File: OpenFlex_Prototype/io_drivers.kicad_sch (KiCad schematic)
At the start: 29 parts, among them Q1 IRF740, Q2 IRF740, Q3 IRF740, Q4 IRF740, U1 LM324, U2 TC4424, U3 TC4424

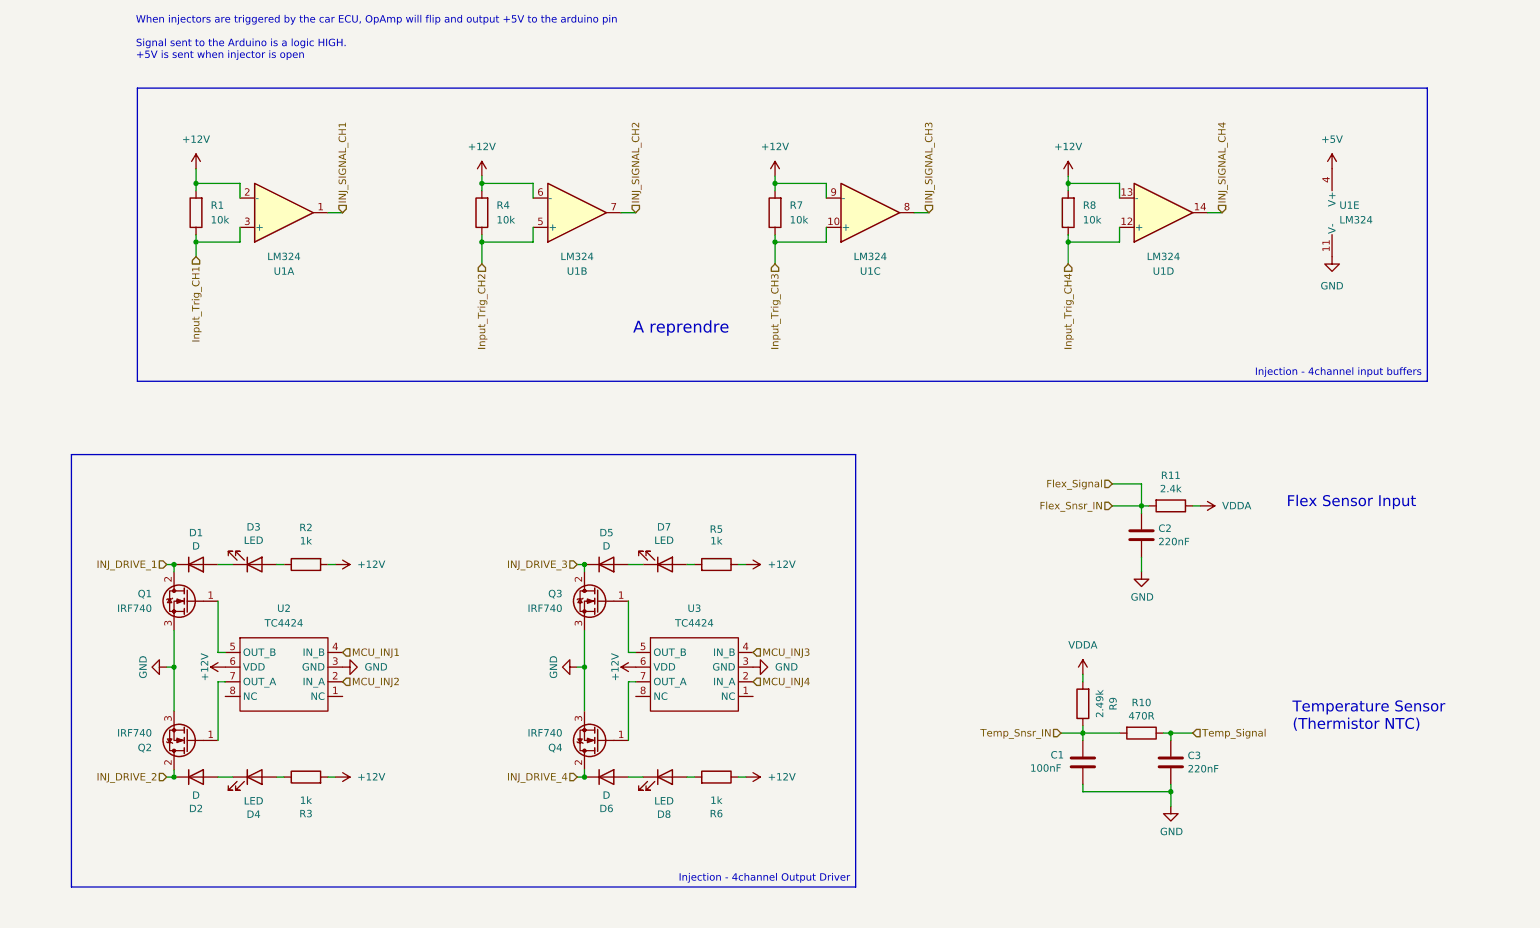
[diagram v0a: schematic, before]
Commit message: Updated PCB to ESP32-S2-Devkit-C1
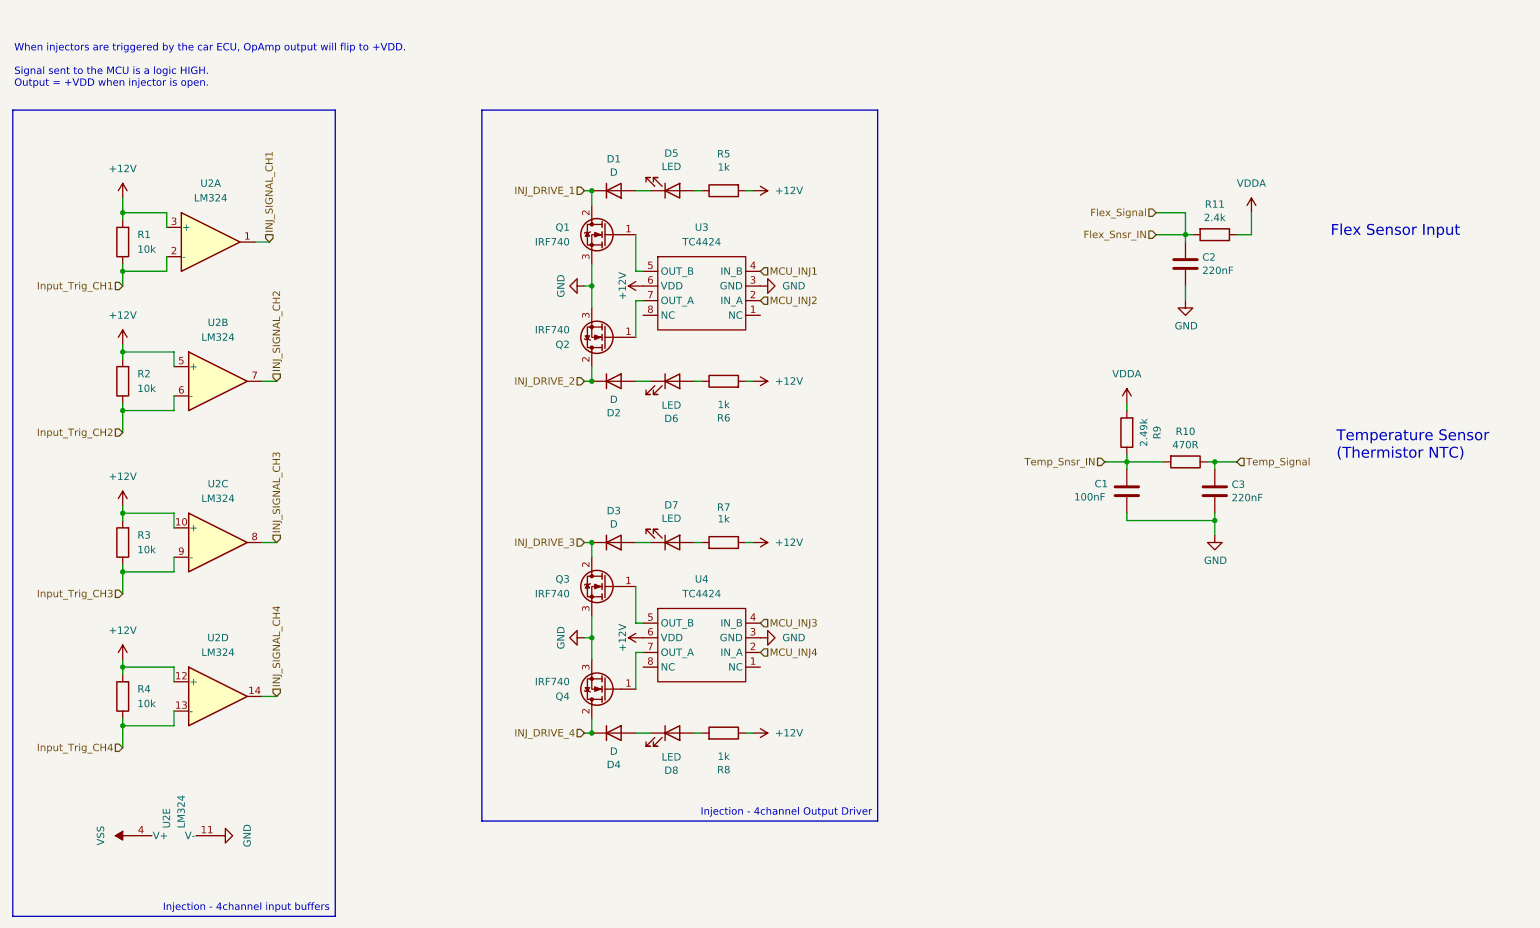
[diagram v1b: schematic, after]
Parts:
- Q1, Q2, Q3, Q4: Manufacturer_Name (none) -> Vishay Semiconductors; Manufacturer_Part_Number (none) -> IRF740PBF; Mouser_Part_Number (none) -> 844-IRF740PBF; URL (none) -> https://www.mouser.fr/ProductDetail/Vishay-Semiconductors/I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
- renumbered D5 to D3, D6 to D4, D3 to D5, D4 to D6, R4 to R2, R7 to R3, R8 to R4, R2 to R5, R3 to R6, R5 to R7, R6 to R8, U1 to U2, U2 to U3, U3 to U4
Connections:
- net +12V: now also U2.10 (+), U2.12 (+), U2.3 (+), U2.5 (+); no longer U2.13 (-), U2.2 (-), U2.6 (-), U2.9 (-)
- net Input_Trig_CH1: now also U2.2 (-); no longer U2.3 (+)
- net Input_Trig_CH2: now also U2.6 (-); no longer U2.5 (+)
- net Input_Trig_CH3: now also U2.9 (-); no longer U2.10 (+)
- net Input_Trig_CH4: now also U2.13 (-); no longer U2.12 (+)
- net +5V renamed VSS
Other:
- note added: "When injectors are triggered by the car ECU, OpAmp output will flip to +VDD. Signal sent to the MCU is a logic HIGH. Output = +VDD when injector is open."
- note removed: "A reprendre"
- note removed: "When injectors are triggered by the car ECU, OpAmp will flip and output +5V to the arduino pin Signal sent to the Arduino is a logic HIGH. +5V is sent when injector is open"
- moved on the sheet: C1, C2, C3, D1, D2, D3, D4, D5, D6, D7, D8, Q4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

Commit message: Updated Sourcing for prototype
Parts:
- C1: Digikey Part Number 445-180563-1-ND -> (none); URL https://www.digikey.com.au/product-detail/en/tdk-corporatio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 -> https://www.mouser.fr/ProductDetail/TDK/FA18X8R1E104KNU06?q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
- C2, C3: Digikey Part Number Digikey Part Number -> (none); URL https://www.digikey.com.au/product-detail/en/tdk-corporatio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 -> https://www.mouser.fr/ProductDetail/TDK/FA18X8R1E224KRU06?q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
- D7: Digikey Part Number 732-5005-ND -> (none)
- R1, R2, R3, R4: Manufacturer_Name (none) -> YAGEO; Manufacturer_Part_Number (none) -> MFR-25FBF52-10K; Mouser_Part_Number (none) -> 603-MFR-25FBF52-10K; URL (none) -> https://www.mouser.fr/ProductDetail/YAGEO/MFR-25FBF52-10K?q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
- R10: Digikey Part Number P470CCT-ND -> (none); Manufacturer_Name Panasonic -> YAGEO; Manufacturer_Part_Number ERJ-6ENF4700V -> MFR-25FTE52-470R; Mouser_Part_Number (none) -> 603-MFR-25FTE52-470R; URL https://www.digikey.com/product-detail/en/panasonic-electro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 -> https://www.mouser.fr/ProductDetail/YAGEO/MFR-25FTE52-470R?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
- R11: Digikey Part Number 311-2.40KCRCT-ND -> (none); Manufacturer_Part_Number RC0805FR-072K4L -> MFR-25FBF52-2K4; Mouser_Part_Number (none) -> 603-MFR-25FBF52-2K4; URL https://www.digikey.com/product-detail/en/yageo/RC0805FR-07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 -> https://www.mouser.fr/ProductDetail/YAGEO/MFR-25FBF52-2K4?q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
- R5, R6, R7, R8: Digikey Part Number 311-1.00KCRCT-ND -> (none); Manufacturer_Name Yageo -> YAGEO; Manufacturer_Part_Number RC0805FR-071KL -> MFR-25FBF52-1K; Mouser_Part_Number (none) -> 603-MFR-25FBF52-1K; URL https://www.digikey.com/product-detail/en/yageo/RC0805FR-07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 -> https://www.mouser.fr/ProductDetail/YAGEO/MFR-25FBF52-1K?qs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
- R9: Digikey Part Number YAG1854CT-ND -> (none); Manufacturer_Part_Number RT0805BRD072K49L -> MFR-25FBF52-2K49; Mouser_Part_Number (none) -> 603-MFR-25FBF52-2K49; URL https://www.digikey.com/product-detail/en/yageo/RT0805BRD07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 -> https://www.mouser.fr/ProductDetail/YAGEO/MFR-25FBF52-2K49?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
- U2: Manufacturer Texas Instrument -> (none); Manufacturer part number LM324KAN -> (none); Manufacturer_Name (none) -> Texas Instrument; Manufacturer_Part_Number (none) -> LM324KAN; Mouser link https://www.mouser.fr/ProductDetail/Texas-Instruments/LM324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 -> (none); Mouser part Number 595-LM324KAN -> (none); Mouser_Part_Number (none) -> 595-LM324KAN; URL (none) -> https://www.mouser.fr/ProductDetail/Texas-Instruments/LM324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
- U3, U4: Manufacturer Microchip Technology -> (none); Manufacturer part number TC4424AVPA -> (none); Manufacturer_Name (none) -> Microchip Technology; Manufacturer_Part_Number (none) -> TC4424AVPA; Mouser link https://www.mouser.fr/ProductDetail/Microchip-Technology/TC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 -> (none); Mouser part number 579-TC4424AVPA -> (none); Mouser_Part_Number (none) -> 579-TC4424AVPA; URL (none) -> https://www.mouser.fr/ProductDetail/Microchip-Technology/TC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
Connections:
- net +12V: now also R5.1, R6.1; no longer R5.2, R6.2
- net at D5.2 (A): now also R5.2; no longer R5.1
- net at D6.2 (A): now also R6.2; no longer R6.1
- no-connect marks 0 -> 4

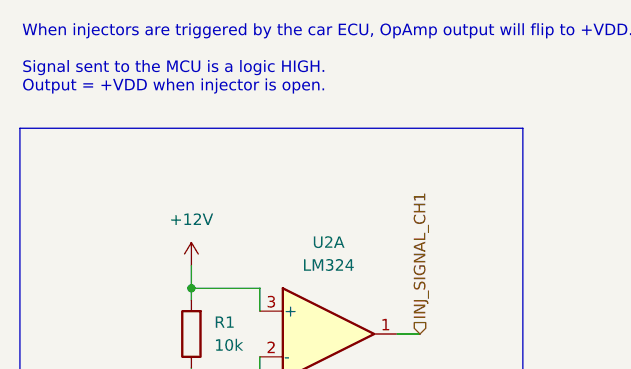
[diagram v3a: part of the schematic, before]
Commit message: Actualized file name
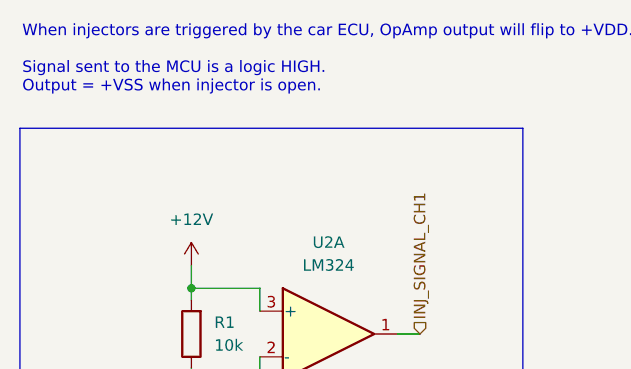
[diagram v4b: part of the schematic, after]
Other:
- note added: "When injectors are triggered by the car ECU, OpAmp output will flip to +VDD. Signal sent to the MCU is a logic HIGH. Output = +VSS when injector is open."
- note removed: "When injectors are triggered by the car ECU, OpAmp output will flip to +VDD. Signal sent to the MCU is a logic HIGH. Output = +VDD when injector is open."

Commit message: Updated BOM
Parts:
- removed Q1, Q2, Q3, Q4: IRF740, Package_TO_SOT_THT:TO-220-3_Horizontal_TabDown, symbol Transistor_FET:IRF740
- added Q1, Q2, Q3, Q4: STP80NF55-08, Package_TO_SOT_THT:TO-220-3_Horizontal_TabDown, symbol Transistor_FET:Q_NMOS_GDS
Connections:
- net GND: now also Q1.3 (S), Q2.3 (S), Q3.3 (S), Q4.3 (S)
- net INJ_DRIVE_1: now also Q1.2 (D)
- net INJ_DRIVE_2: now also Q2.2 (D)
- net INJ_DRIVE_3: now also Q3.2 (D)
- net INJ_DRIVE_4: now also Q4.2 (D)
- net at U4.5 (OUT_B): now also Q3.1 (G)
- net at U4.7 (OUT_A): now also Q4.1 (G)
- net at U3.5 (OUT_B): now also Q1.1 (G)
- net at U3.7 (OUT_A): now also Q2.1 (G)
